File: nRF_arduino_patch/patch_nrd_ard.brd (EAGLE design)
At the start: 22 x 18.3 mm, 14 parts

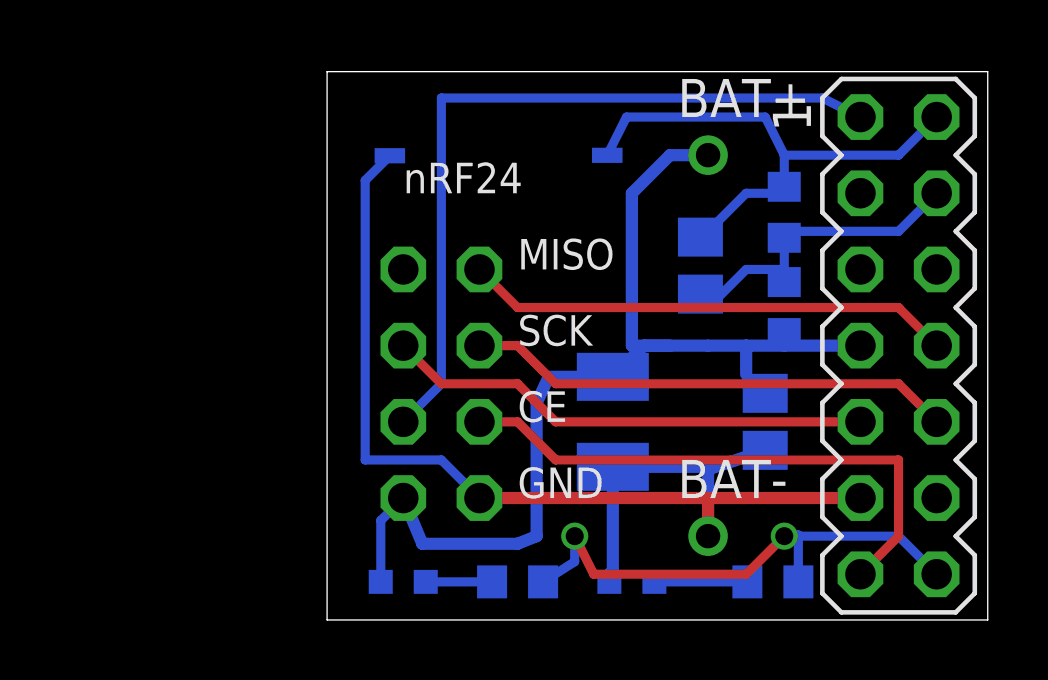
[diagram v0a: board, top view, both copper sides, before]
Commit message: added  Nano Modem some modifications on nRFPatch board
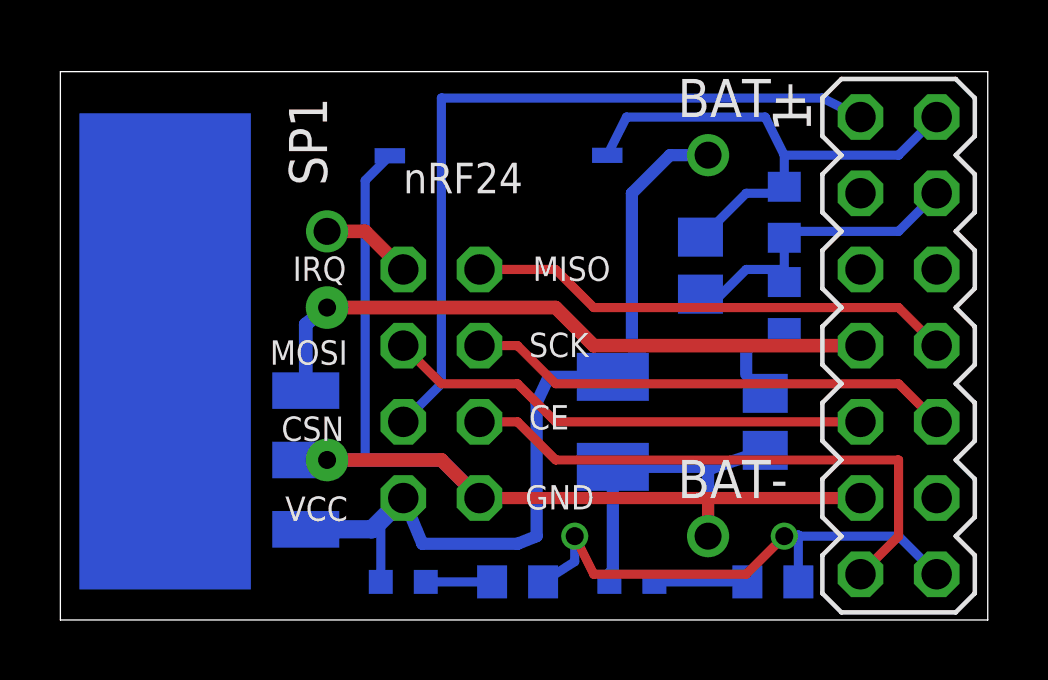
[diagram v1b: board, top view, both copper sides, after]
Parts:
- added IC1: 3.3V, 1AA_Stofer:SOT223
- added SP1: SOLDER_POINTA, 1AA_Stofer:P1-13
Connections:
- new net VCC_5V: IC1.1, SV1.7
- net GND: now also IC1.2
- net IRQ: now also SP1.1
- net VCC3_3: now also IC1.3; no longer SV1.7
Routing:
- net VCC_5V: track 0.00 -> 21.4 mm, vias 0 -> 1
- net GND: track 41.2 -> 49.3 mm, vias 0 -> 1
- net IRQ: track 0.00 -> 3.07 mm
- net VCC3_3: track 36.5 -> 37.7 mm
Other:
- board size 22 x 18.3 mm -> 30.9 x 18.3 mm
- board text added: "CSN"
- board text added: "IRQ"
- board text added: "MOSI"
- board text added: "VCC"

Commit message: Added  Nrf24 Arduino Mysensor node
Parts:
- C2: value 0.uf -> 0.1uf
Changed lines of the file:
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@@
 <attribute name="NAME" x="52.07" y="28.575" size="1.016" layer="26" rot="MR270"/>
 </element>
-<element name="C2" library="rcl" package="C0805" value="0.uf " x="59.055" y="27.94" smashed="yes" rot="MR270">
+<element name="C2" library="rcl" package="C0805" value="0.1uf " x="59.055" y="27.94" smashed="yes" rot="MR270">
 <attribute name="NAME" x="57.785" y="28.575" size="1.016" layer="26" rot="MR270"/>
 <attribute name="VALUE" x="61.595" y="29.21" size="1.27" layer="28" rot="MR270"/>

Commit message: nRF_arduino_patch: Fixed swapped values on R2/R3
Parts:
- R2: value 470K -> 1M
- R3: value 1M -> 470K
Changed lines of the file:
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@@
 <element name="BAT+" library="1AA_Stofer" package="P1-13" value="SOLDER_POINTA" x="57.15" y="36.83"/>
 <element name="BAT-" library="1AA_Stofer" package="P1-13" value="SOLDER_POINTA" x="57.15" y="24.13"/>
-<element name="R2" library="rcl" package="R0603" value="470K" x="59.69" y="31.75" smashed="yes" rot="MR270">
+<element name="R2" library="rcl" package="R0603" value="1M" x="59.69" y="31.75" smashed="yes" rot="MR270">
 <attribute name="NAME" x="58.42" y="32.385" size="1.016" layer="26" rot="MR270"/>
 </element>
-<element name="R3" library="rcl" package="R0603" value="1M" x="59.69" y="34.925" smashed="yes" rot="MR270">
+<element name="R3" library="rcl" package="R0603" value="470K" x="59.69" y="34.925" smashed="yes" rot="MR270">
 <attribute name="NAME" x="58.42" y="35.56" size="1.016" layer="26" rot="MR270"/>
 </element>
